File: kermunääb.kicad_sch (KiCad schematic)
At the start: 135 parts, among them J1 Conn_01x05, SW1 RotaryEncoder_Switch, SW10 SW_SPST, SW11 SW_SPST, SW12 SW_SPST, SW13 SW_SPST, SW14 SW_SPST, SW15 SW_SPST, SW16 SW_SPST, SW17 SW_SPST, SW18 SW_SPST, SW19 SW_SPST, SW2 SW_SPST, SW20 SW_SPST, SW21 SW_SPST, SW22 SW_SPST, SW23 SW_SPST, SW24 SW_SPST, SW25 SW_SPST, SW26 SW_SPST, SW27 SW_SPST, SW28 SW_SPST, SW29 SW_SPST, SW3 SW_SPST, SW30 SW_SPST, SW31 SW_SPST, SW32 SW_SPST, SW33 SW_SPST, SW33A1 SW_SPST, SW34 SW_SPST, SW35 SW_SPST, SW36 SW_SPST, SW37 SW_SPST, SW38 SW_SPST, SW39 SW_SPST, SW4 SW_SPST, SW40 SW_SPST, SW41 SW_SPST, SW42 SW_SPST, SW43 SW_SPST, SW44 SW_SPST, SW45 SW_SPST, SW46 SW_SPST, SW47 SW_SPST, SW48 SW_SPST, SW49 SW_SPST, SW5 SW_SPST, SW50 SW_SPST, SW51 SW_SPST, SW52 SW_SPST, SW53 SW_SPST, SW54 SW_SPST, SW55 SW_SPST, SW56 SW_SPST, SW57 SW_SPST, SW58 SW_SPST, SW59 SW_SPST, SW6 SW_SPST, SW60 SW_SPST, SW61 SW_SPST, SW62 SW_SPST, SW63 SW_SPST, SW64 SW_SPST, SW65 SW_SPST, SW7 SW_SPST, SW8 SW_SPST, SW9 SW_SPST, U1 ProMicro, U2 ProMicro

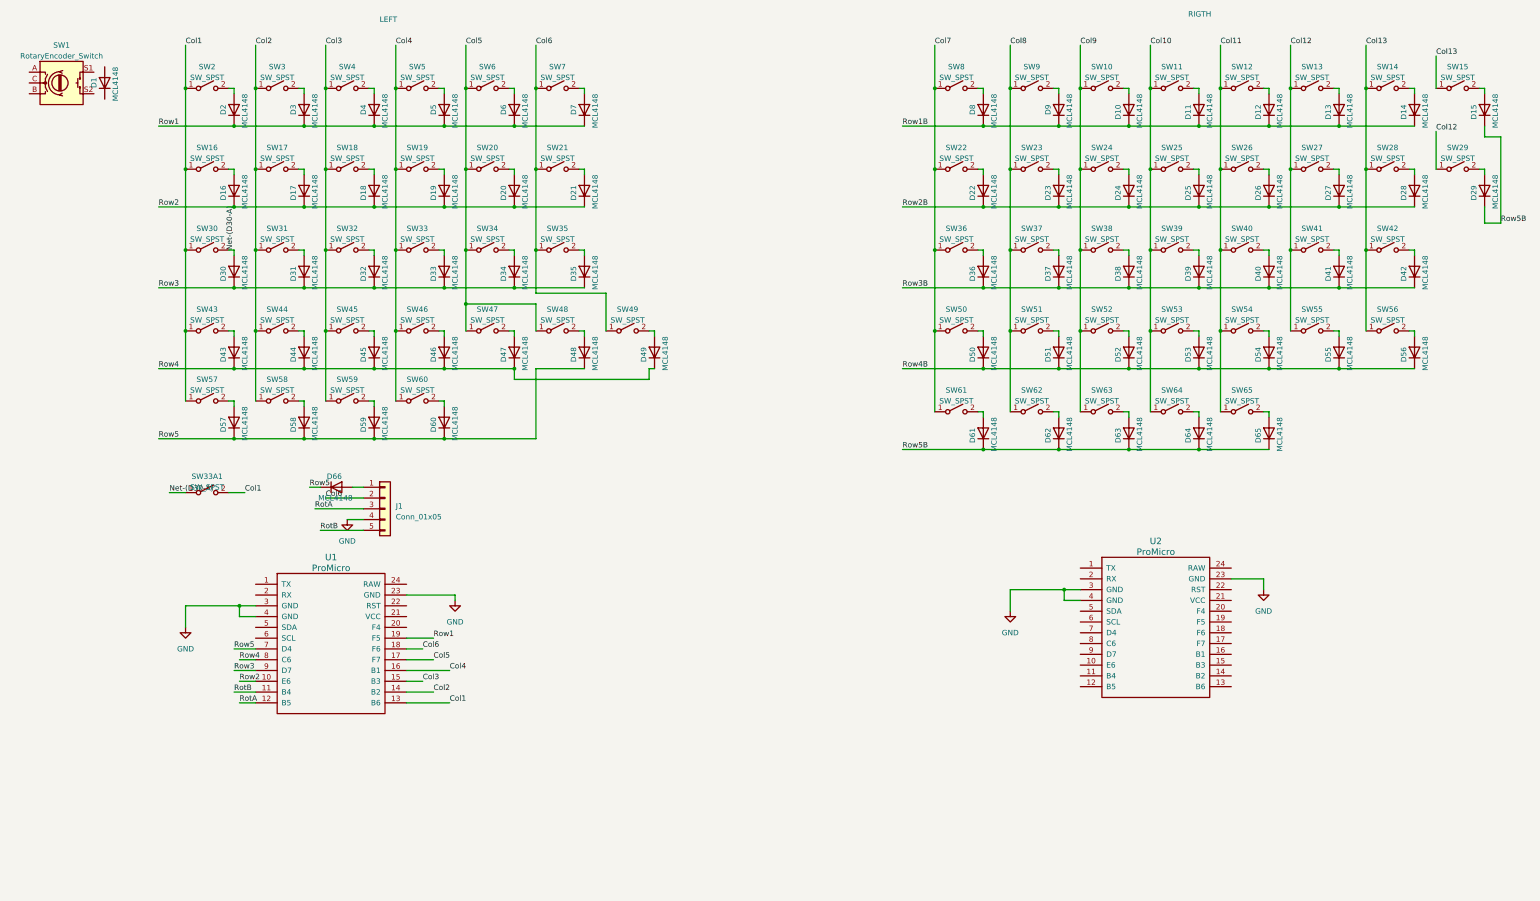
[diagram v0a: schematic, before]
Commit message: initial routing for right half and tweaks
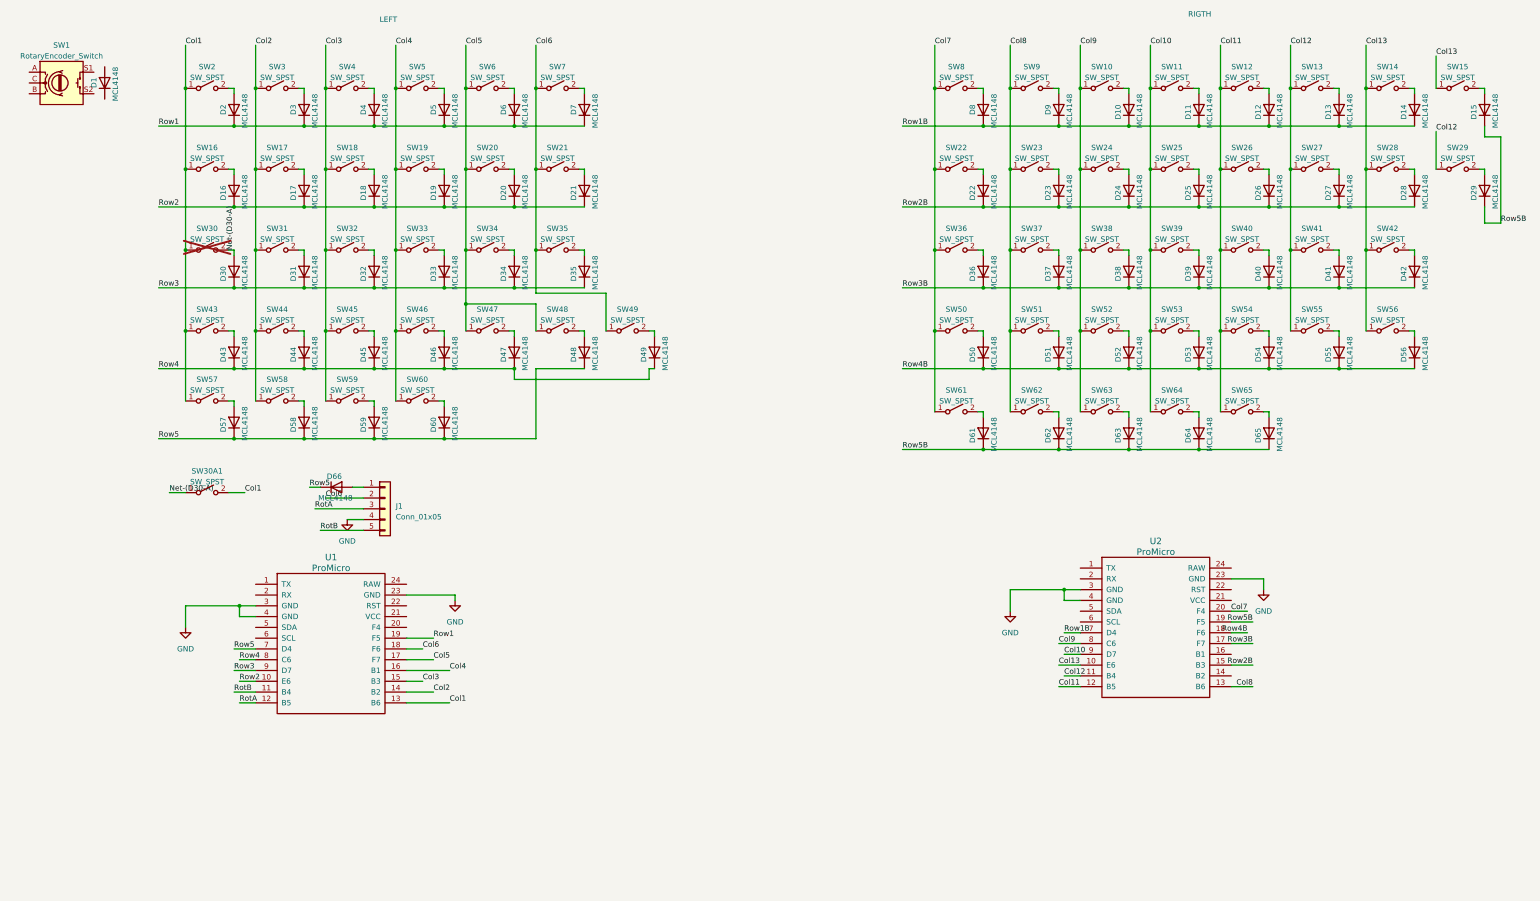
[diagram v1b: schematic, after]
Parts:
- SW30: now not fitted
- U2: footprint (none) -> promicro:ProMicro
- renumbered SW33A1 to SW30A1
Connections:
- net Col10: now also U2.9 (D7)
- net Col11: now also U2.12 (B5)
- net Col12: now also U2.11 (B4)
- net Col13: now also U2.10 (E6)
- net Col7: now also U2.20 (F4)
- net Col8: now also U2.13 (B6)
- net Col9: now also U2.8 (C6)
- net Row1B: now also U2.7 (D4)
- net Row2B: now also U2.15 (B3)
- net Row3B: now also U2.17 (F7)
- net Row4B: now also U2.18 (F6)
- net Row5B: now also U2.19 (F5)
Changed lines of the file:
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@@
     (stroke (width 0) (type default))
   )
+  (wire (pts (xy 267.97 201.93) (xy 273.05 201.93))
+    (stroke (width 0) (type default))
+  )
   (wire (pts (xy 317.5 107.95) (xy 334.01 107.95))
     (stroke (width 0) (type default))
@@
     (stroke (width 0) (type default))
   )
+  (wire (pts (xy 308.61 201.93) (xy 313.69 201.93))
+    (stroke (width 0) (type default))
+  )
   (wire (pts (xy 248.92 137.16) (xy 250.19 137.16))
     (stroke (width 0) (type default))
@@
     (stroke (width 0) (type default))
   )
+  (wire (pts (xy 308.61 186.69) (xy 313.69 186.69))
+    (stroke (width 0) (type default))
+  )
   (wire (pts (xy 256.54 99.06) (xy 256.54 118.11))
     (stroke (width 0) (type default))
@@
     (stroke (width 0) (type default))
   )
+  (wire (pts (xy 308.61 189.23) (xy 312.42 189.23))
+    (stroke (width 0) (type default))
+  )
   (wire (pts (xy 256.54 184.15) (xy 256.54 179.07))
     (stroke (width 0) (type default))
@@
     (stroke (width 0) (type default))
   )
+  (wire (pts (xy 267.97 196.85) (xy 273.05 196.85))
+    (stroke (width 0) (type default))
+  )
   (wire (pts (xy 121.92 118.11) (xy 123.19 118.11))
     (stroke (width 0) (type default))
@@
     (stroke (width 0) (type default))
   )
+  (wire (pts (xy 308.61 191.77) (xy 313.69 191.77))
+    (stroke (width 0) (type default))
+  )
   (wire (pts (xy 273.05 181.61) (xy 269.24 181.61))
     (stroke (width 0) (type default))
@@
     (stroke (width 0) (type default))
   )
+  (wire (pts (xy 269.24 194.31) (xy 273.05 194.31))
+    (stroke (width 0) (type default))
+  )
   (wire (pts (xy 340.36 80.01) (xy 340.36 99.06))
     (stroke (width 0) (type default))
@@
     (stroke (width 0) (type default))
   )
+  (wire (pts (xy 267.97 191.77) (xy 273.05 191.77))
+    (stroke (width 0) (type default))
+  )
   (wire (pts (xy 154.94 60.96) (xy 156.21 60.96))
     (stroke (width 0) (type default))
@@
     (stroke (width 0) (type default))
   )
+  (wire (pts (xy 269.24 199.39) (xy 273.05 199.39))
+    (stroke (width 0) (type default))
+  )
   (wire (pts (xy 55.88 107.95) (xy 73.66 107.95))
     (stroke (width 0) (type default))
@@
     (stroke (width 0) (type default))
   )
+  (wire (pts (xy 269.24 189.23) (xy 273.05 189.23))
+    (stroke (width 0) (type default))
+  )
   (wire (pts (xy 231.14 146.05) (xy 250.19 146.05))
     (stroke (width 0) (type default))
@@
     (stroke (width 0) (type default))
   )
+  (wire (pts (xy 308.61 196.85) (xy 313.69 196.85))
+    (stroke (width 0) (type default))
+  )
   (wire (pts (xy 139.7 80.01) (xy 139.7 81.28))
     (stroke (width 0) (type default))
@@
     (stroke (width 0) (type default))
   )
+  (wire (pts (xy 308.61 184.15) (xy 312.42 184.15))
+    (stroke (width 0) (type default))
+  )
   (wire (pts (xy 156.21 60.96) (xy 156.21 62.23))
     (stroke (width 0) (type default))
@@
     (effects (font (size 1.27 1.27)) (justify left bottom))
   )
+  (label "Row3B" (at 313.69 191.77 180) (fields_autoplaced)
+    (effects (font (size 1.27 1.27)) (justify right bottom))
+  )
   (label "Row4" (at 74.93 195.58 0) (fields_autoplaced)
     (effects (font (size 1.27 1.27)) (justify left bottom))
   )
+  (label "Col12" (at 269.24 199.39 0) (fields_autoplaced)
+    (effects (font (size 1.27 1.27)) (justify left bottom))
+  )
   (label "Col5" (at 120.65 195.58 0) (fields_autoplaced)
     (effects (font (size 1.27 1.27)) (justify left bottom))
@@
     (effects (font (size 1.27 1.27)) (justify left bottom))
   )
+  (label "Col13" (at 267.97 196.85 0) (fields_autoplaced)
+    (effects (font (size 1.27 1.27)) (justify left bottom))
+  )
+  (label "Row1B" (at 269.24 189.23 0) (fields_autoplaced)
+    (effects (font (size 1.27 1.27)) (justify left bottom))
+  )
   (label "Row5B" (at 372.11 92.71 0) (fields_autoplaced)
     (effects (font (size 1.27 1.27)) (justify left bottom))
@@
     (effects (font (size 1.27 1.27)) (justify left bottom))
   )
+  (label "Col11" (at 267.97 201.93 0) (fields_autoplaced)
+    (effects (font (size 1.27 1.27)) (justify left bottom))
+  )
   (label "Col6" (at 118.11 193.04 0) (fields_autoplaced)
     (effects (font (size 1.27 1.27)) (justify left bottom))
@@
     (effects (font (size 1.27 1.27)) (justify left bottom))
   )
+  (label "Col8" (at 313.69 201.93 180) (fields_autoplaced)
+    (effects (font (size 1.27 1.27)) (justify right bottom))
+  )
   (label "Row5" (at 91.44 154.94 0) (fields_autoplaced)
     (effects (font (size 1.27 1.27)) (justify left bottom))
@@
     (effects (font (size 1.27 1.27)) (justify left bottom))
   )
+  (label "Row2B" (at 313.69 196.85 180) (fields_autoplaced)
+    (effects (font (size 1.27 1.27)) (justify right bottom))
+  )
+  (label "Row4B" (at 312.42 189.23 180) (fields_autoplaced)
+    (effects (font (size 1.27 1.27)) (justify right bottom))
+  )
   (label "Row4" (at 55.88 127 0) (fields_autoplaced)
     (effects (font (size 1.27 1.27)) (justify left bottom))
@@
     (effects (font (size 1.27 1.27)) (justify left bottom))
   )
+  (label "Col9" (at 267.97 191.77 0) (fields_autoplaced)
+    (effects (font (size 1.27 1.27)) (justify left bottom))
+  )
   (label "Col12" (at 356.87 71.12 0) (fields_autoplaced)
     (effects (font (size 1.27 1.27)) (justify left bottom))
@@
     (effects (font (size 1.27 1.27)) (justify left bottom))
   )
+  (label "Col7" (at 312.42 184.15 180) (fields_autoplaced)
+    (effects (font (size 1.27 1.27)) (justify right bottom))
+  )
   (label "Col1" (at 76.2 156.21 0) (fields_autoplaced)
     (effects (font (size 1.27 1.27)) (justify left bottom))
   )
+  (label "Col10" (at 269.24 194.31 0) (fields_autoplaced)
+    (effects (font (size 1.27 1.27)) (justify left bottom))
+  )
   (label "RotA" (at 92.71 160.02 0) (fields_autoplaced)
     (effects (font (size 1.27 1.27)) (justify left bottom))
   )
+  (label "Row5B" (at 313.69 186.69 180) (fields_autoplaced)
+    (effects (font (size 1.27 1.27)) (justify right bottom))
+  )
   (label "Row2" (at 74.93 200.66 0) (fields_autoplaced)
     (effects (font (size 1.27 1.27)) (justify left bottom))
@@
   )
   (symbol (lib_id "Switch:SW_SPST") (at 67.31 99.06 0) (unit 1)
-    (in_bom yes) (on_board yes) (dnp no) (fields_autoplaced)
+    (in_bom yes) (on_board yes) (dnp yes) (fields_autoplaced)
     (property "Reference" "SW30" (at 67.31 93.98 0)
       (effects (font (size 1.27 1.27)))
@@
   (symbol (lib_id "Switch:SW_SPST") (at 67.31 156.21 0) (unit 1)
     (in_bom yes) (on_board yes) (dnp no) (fields_autoplaced)
-    (property "Reference" "SW33A1" (at 67.31 152.4 0)
+    (property "Reference" "SW30A1" (at 67.31 151.13 0)
       (effects (font (size 1.27 1.27)))
     )
-    (property "Value" "SW_SPST" (at 67.31 154.94 0)
+    (property "Value" "SW_SPST" (at 67.31 153.67 0)
       (effects (font (size 1.27 1.27)))
     )
@@
       (project "kermunääb"
         (path "/0ccd4a57-3d21-401e-b07c-27b256c43961"
-          (reference "SW33A1") (unit 1)
+          (reference "SW30A1") (unit 1)
         )
       )
@@
       (effects (font (size 1.524 1.524)))
     )
-    (property "Footprint" "" (at 293.37 219.71 0)
+    (property "Footprint" "promicro:ProMicro" (at 293.37 219.71 0)
       (effects (font (size 1.524 1.524)) hide)
     )

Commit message: changed left side to nicenano .gitignore  and added battery wiring, still quite WIP
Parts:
- removed U1: ProMicro, promicro:ProMicro, symbol promicro:ProMicro
- added J2: Conn_01x02_Pin, Connector_JST:JST_XH_S2B-XH-A-1_1x02_P2.50mm_Horizontal, symbol Connector:Conn_01x02_Pin
- added U3, U4: ~, nice-nano-kicad:nice_nanov2_noextras, symbol nice_nano_kicad:nice_nanov2
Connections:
- net Col1: now also U3.14 (P0.09)
- net Col10: now also U4.10 (P1.00)
- net Col11: now also U4.13 (P1.06)
- net Col12: now also U4.12 (P1.04)
- net Col13: now also U4.11 (P0.11)
- net Col2: now also U3.15 (P0.10)
- net Col3: now also U3.16 (P1.11)
- net Col4: now also U3.17 (P1.13)
- net Col5: now also U3.18 (P1.15)
- net Col6: now also U3.19 (P0.02)
- net Col7: now also U4.21 (P0.31)
- net Col8: now also U4.14 (P0.09)
- net Col9: now also U4.9 (P0.24)
- net GND: now also U3.24 (GND), U3.4 (GND), U3.5 (GND), U4.24 (GND), U4.4 (GND), U4.5 (GND)
- net RotA: now also U3.13 (P1.06)
- net RotB: now also U3.12 (P1.04)
- net Row1: now also U3.20 (P0.29)
- net Row1B: now also U4.8 (P0.22)
- net Row2: now also U3.11 (P0.11)
- net Row2B: now also U4.16 (P1.11)
- net Row3: now also U3.10 (P1.00)
- net Row3B: now also U4.18 (P1.15)
- net Row4: now also U3.9 (P0.24)
- net Row5: now also U3.8 (P0.22)
- net Row5B: now also U4.20 (P0.29)
- new net BAT+: J2.2 (Pin_2), U3.25 (BAT+)
- new net BAT-: J2.1 (Pin_1), U3.1 (GND)
